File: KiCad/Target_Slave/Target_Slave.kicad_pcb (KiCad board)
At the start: 2 copper layers, 76.2 x 50.8 mm, 44 parts, among them J1 ICSP, J2 I2C, J3 I2C, SW1 I2C Address, U1 PIC16F1788-IP, U2 TSSP4038, U3 TSOP53456

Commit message: Rev B Target Slave PCB design
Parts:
- removed ? (x3): , 
- removed D6: LED, LED_SMD:LED_0805_2012Metric_Pad1.15x1.40mm_HandSolder
- removed the G*** at (135.4, 83.2)
- removed the G*** at (132.0, 118.1)
- removed the G*** at (121.2, 112.8)
- removed R10, R12: 90Ω, Resistor_SMD:R_0805_2012Metric_Pad1.20x1.40mm_HandSolder
- removed R11: 150Ω, Resistor_SMD:R_0805_2012Metric_Pad1.20x1.40mm_HandSolder
- removed R13: 4.7kΩ, Resistor_SMD:R_0805_2012Metric_Pad1.20x1.40mm_HandSolder
- removed R6, R7, R8: 330Ω, Resistor_SMD:R_0805_2012Metric_Pad1.20x1.40mm_HandSolder
- removed R9: 10kΩ, Resistor_SMD:R_0805_2012Metric_Pad1.20x1.40mm_HandSolder
- removed the REF** at (183.6, 81.9)
- removed SW1: I2C Address, 0_AKeller_Footprints:SW_DIP_SPSTx08_Slide_9.78x22.5mm_W7.62mm_P2.54mm
- removed U3: TSOP53456, 0_AKeller_Footprints:IR Receiver
- added C7: 1µF, Capacitor_SMD:C_0805_2012Metric_Pad1.18x1.45mm_HandSolder, F.Cu at (233.9, 81.3)
- added C8: 22uF, Capacitor_SMD:C_0805_2012Metric_Pad1.18x1.45mm_HandSolder, F.Cu at (234.9, 63.9)
- added C9: 0.1uF, Capacitor_SMD:C_0805_2012Metric_Pad1.18x1.45mm_HandSolder, F.Cu at (239.5, 63.9)
- added G***: LOGO, 2025 Logos:AKeller_Logo_0-23x0-31, F.Cu at (243.0, 56.4)
- added G***: LOGO, 2025 Logos:RCET Stacked 0-25x0_76, F.Cu at (218.3, 83.8)
- added J10: I2C, 0_AKeller_Footprints:1x6_100mil_Header, F.Cu at (214.6, 48.9)
- added J4: I2C, 0_AKeller_Footprints:1x6_100mil_Header, F.Cu at (248.9, 70.5)
- added J5: SERVO1, 0_AKeller_Footprints:1x3_100mil_Header, F.Cu at (234.9, 92.1)
- added J6: SERVO3, 0_AKeller_Footprints:1x3_100mil_Header, F.Cu at (234.9, 76.8)
- added J7: SERVO2, 0_AKeller_Footprints:1x3_100mil_Header, F.Cu at (234.9, 84.5)
- added J8: Stepper, 0_AKeller_Footprints:1x4_100mil_Header, F.Cu at (193.0, 92.1)
- added J9: I2C, 0_AKeller_Footprints:1x6_100mil_Header, F.Cu at (214.6, 92.1)
- added JP1: Mode, 0_AKeller_Footprints:1x3_100mil_Jumper, F.Cu at (214.6, 61.6)
- added REF**: M3 Mounting, 0_AKeller_Footprints:M3 Mounting, F.Cu at (180.3, 92.1)
- added REF**: M3 Mounting, 0_AKeller_Footprints:M3 Mounting, F.Cu at (248.9, 92.1)
- added REF**: M3 Mounting, 0_AKeller_Footprints:M3 Mounting, F.Cu at (180.3, 48.9)
- added REF**: M3 Mounting, 0_AKeller_Footprints:M3 Mounting, F.Cu at (248.9, 48.9)
- added TP10: PWR, 0_AKeller_Footprints:1x1_100mil_Header, F.Cu at (239.4, 69.8)
- added TP5: IR, 0_AKeller_Footprints:1x1_100mil_Header, F.Cu at (220.0, 56.9)
- added TP6: TX, 0_AKeller_Footprints:1x1_100mil_Header, F.Cu at (190.0, 59.1)
- added TP7: SCL, 0_AKeller_Footprints:1x1_100mil_Header, F.Cu at (201.8, 85.9)
- added TP8: SDA, 0_AKeller_Footprints:1x1_100mil_Header, F.Cu at (205.6, 85.9)
- added TP9: RX, 0_AKeller_Footprints:1x1_100mil_Header, F.Cu at (207.5, 67.2)
- C4: value 1uF -> 1µF
- C5: value 22uF -> 1µF
- C6: value 0.1uF -> 1µF
- D1: footprint 0_AKeller_Footprints:Diode_0805 -> Diode_SMD:D_0805_2012Metric_Pad1.15x1.40mm_HandSolder
- D2: value IN-P32TRRRGB -> WS2812B; footprint 0_AKeller_Footprints:IN-P32TRRRGB -> LED_SMD:LED_WS2812B_PLCC4_5.0x5.0mm_P3.2mm; moved to F.Cu
- D3: value IN-P32TRRRGB -> Enable; footprint 0_AKeller_Footprints:IN-P32TRRRGB -> LED_SMD:LED_0805_2012Metric_Pad1.15x1.40mm_HandSolder; moved to F.Cu
- D4: value IN-P32TRRRGB -> Hit; footprint 0_AKeller_Footprints:IN-P32TRRRGB -> LED_SMD:LED_0805_2012Metric_Pad1.15x1.40mm_HandSolder; moved to F.Cu
- D5: value IN-P32TRRRGB -> Power; footprint 0_AKeller_Footprints:IN-P32TRRRGB -> LED_SMD:LED_0805_2012Metric_Pad1.15x1.40mm_HandSolder; moved to F.Cu
- J2: value I2C -> LED; footprint 0_AKeller_Footprints:1x4_100mil_Header -> 0_AKeller_Footprints:1x3_100mil_Header_Locking
- J3: footprint 0_AKeller_Footprints:1x4_100mil_Header -> 0_AKeller_Footprints:1x6_100mil_Header
- R1: value 330Ω -> 10kΩ
- R2: value 330Ω -> 470Ω
- R3, R4, R5: value 330Ω -> 4.7kΩ
- TP1: value ~ -> MCLR
- TP2: value ~ -> RGB_IN
- TP3: value ~ -> Enable
- TP4: value ~ -> Hit
- moved C5 115.9 mm to (233.9, 69.8), turned to 0 degrees
- moved R2 114.9 mm to (224.3, 58.5), turned to 0 degrees
- moved D5 107.5 mm to (230.1, 64.9), turned to 0 degrees
- moved D2 105.6 mm to (233.1, 56.9)
- moved TP2 85.9 mm to (202.4, 61.5)
- moved C4 85.2 mm to (233.9, 88.9), turned to 0 degrees
- moved R1 84.4 mm to (188.7, 67.0)
- moved R5 81.6 mm to (224.8, 64.9), turned to 180 degrees
- moved J2 73.6 mm to (235.6, 48.9), turned to 0 degrees
- moved C6 72.5 mm to (197.9, 87.9), turned to 180 degrees
- moved R4 71.6 mm to (187.7, 72.4), turned to 180 degrees
- moved R3 71.1 mm to (187.7, 77.5), turned to 180 degrees
- moved D1 70.7 mm to (196.3, 67.0)
- moved J3 69.5 mm to (180.3, 70.5), turned to -90 degrees
- moved U2 69.3 mm to (220.0, 70.5), turned to -90 degrees
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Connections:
- net RB6 renamed TX
- C4 pad 1: +5V -> GND
- C4 pad 2: GND -> +5V
- C5 pad 1: +5V -> GND
- C5 pad 2: GND -> +5V
- C6 pad 1: +5V -> GND
- C6 pad 2: GND -> +5V
- D1 pad 1: Net-(D1-K) -> /MCLR
- D2 pad 1: Net-(D2-BK) -> +5V
- D2 pad 2: Net-(D2-GK) -> Net-(D2-DOUT)
- D2 pad 3: Net-(D2-RK) -> GND
- D2 pad 4: +5V -> Net-(D2-DIN)
- D3 pad 1: Net-(D2-BK) -> Net-(D3-K)
- D3 pad 2: Net-(D2-GK) -> Net-(D3-A)
- D4 pad 1: Net-(D2-BK) -> Net-(D4-K)
- D4 pad 2: Net-(D2-GK) -> Net-(D4-A)
- D5 pad 1: Net-(D2-BK) -> Net-(D5-K)
- D5 pad 2: Net-(D2-GK) -> +5V
- J1 pad 1: Net-(D1-K) -> /MCLR
- J1 pad 4: RB7 -> RX
- J2 pad 2: Net-(U1-RC3/SCK/SCL) -> Net-(D2-DOUT)
- J2 pad 3: Net-(U1-RC4/SDI/SDA) -> GND
- J3 pad 2: Net-(U1-RC3/SCK/SCL) -> +5V
- J3 pad 3: Net-(U1-RC4/SDI/SDA) -> /SCL
- J3 pad 4: GND -> /SDA
- R1 pad 1: GND -> +5V
- R1 pad 2: /RA0 -> Net-(D1-A)
- R2 pad 1: GND -> Net-(U1-ULPWU/C12IN0-/AN0/RA0)
- R2 pad 2: /RA1 -> Net-(D2-DIN)
- R3 pad 1: GND -> Net-(D3-K)
- R3 pad 2: /RA2 -> GND
- R4 pad 1: GND -> Net-(D4-K)
- R4 pad 2: /RA3 -> GND
- R5 pad 1: GND -> Net-(D5-K)
- R5 pad 2: /RA4 -> GND
- TP1 pad 1: Net-(U1-INT/AN12/RB0) -> /MCLR
- TP2 pad 1: Net-(U1-RC3/SCK/SCL) -> Net-(U1-ULPWU/C12IN0-/AN0/RA0)
- TP3 pad 1: Net-(U1-RC4/SDI/SDA) -> Net-(D3-A)
- TP4 pad 1: Net-(U1-P1C/AN10/RB1) -> Net-(D4-A)
- U1 pad 1: Net-(D1-K) -> /MCLR
- U1 pad 10: /RA6 -> Net-(U1-CLKIN/OSC1/RA7)
- U1 pad 11: unconnected-(U1-RC0/T1OSO/T1CK1-Pad11) -> SERVO1
- U1 pad 13: unconnected-(U1-RC2/P1A/CCP1-Pad13) -> STEP
- U1 pad 14: Net-(U1-RC3/SCK/SCL) -> /SCL
- U1 pad 15: Net-(U1-RC4/SDI/SDA) -> /SDA
- U1 pad 16: unconnected-(U1-RC5/SDO-Pad16) -> SERVO3
- U1 pad 17: unconnected-(U1-RC6/TX/CK-Pad17) -> SERVO2
- U1 pad 2: /RA0 -> Net-(U1-ULPWU/C12IN0-/AN0/RA0)
- U1 pad 21: Net-(U1-INT/AN12/RB0) -> unconnected-(U1-INT/AN12/RB0-Pad21)
- U1 pad 22: Net-(U1-P1C/AN10/RB1) -> unconnected-(U1-P1C/AN10/RB1-Pad22)
- U1 pad 23: Net-(U1-P1B/AN8/RB2) -> unconnected-(U1-P1B/AN8/RB2-Pad23)
- U1 pad 24: Net-(U1-PGM/C12IN2-/AN8/RB3) -> unconnected-(U1-PGM/C12IN2-/AN8/RB3-Pad24)
- U1 pad 25: Net-(U1-P1D/AN11/RB4) -> unconnected-(U1-P1D/AN11/RB4-Pad25)
- U1 pad 28: RB7 -> Net-(JP1-C)
- U1 pad 3: /RA1 -> Net-(D4-A)
- U1 pad 4: /RA2 -> Net-(D3-A)
- U1 pad 5: /RA3 -> DIR
- U1 pad 6: /RA4 -> unconnected-(U1-T0CKI/C1OUT/RA4-Pad6)
- U1 pad 7: /RA5 -> unconnected-(U1-~{SS}/C2OUT/AN4/RA5-Pad7)
- U1 pad 9: /RA7 -> Net-(U1-CLKIN/OSC1/RA7)
- U2 pad 1: Net-(U1-INT/AN12/RB0) -> Net-(JP1-A)
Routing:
- net /SDA: track 0.00 -> 201.2 mm
- net /SCL: track 0.00 -> 193.1 mm
- net Net-(U1-RC3/SCK/SCL): track 151.6 -> 0.00 mm
- net Net-(U1-RC4/SDI/SDA): track 133.8 -> 0.00 mm
- net Net-(D2-GK): track 97.1 -> 0.00 mm, vias 1 -> 0
- net Net-(D2-RK): track 95.8 -> 0.00 mm
- net Net-(D2-BK): track 92.1 -> 0.00 mm, vias 1 -> 0
- net +5V: track 280.4 -> 226.8 mm
- net SERVO1: track 0.00 -> 43.0 mm
- net Net-(D1-K): track 41.8 -> 0.00 mm
- net SERVO2: track 0.00 -> 40.0 mm
- net Net-(U1-ULPWU/C12IN0-/AN0/RA0): track 0.00 -> 37.3 mm
- net /MCLR: track 0.00 -> 36.0 mm
- net RB7: track 35.2 -> 0.00 mm
- net /RA7: track 31.8 -> 0.00 mm, vias 1 -> 0
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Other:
- board text added: "Game"
- board text added: "Laser Arcade Target Slave Rev. B - Fall 2025"
- board text added: "PGM"
- board text added: "SIG"
- board text removed: "D2"
- board text removed: "D3"
- board text removed: "D4"
- board text removed: "D5"
- board text removed: "I2C"
- board text removed: "ICSP"
- board text removed: "Laser Arcade Target Slave Rev. A Spring 2025"

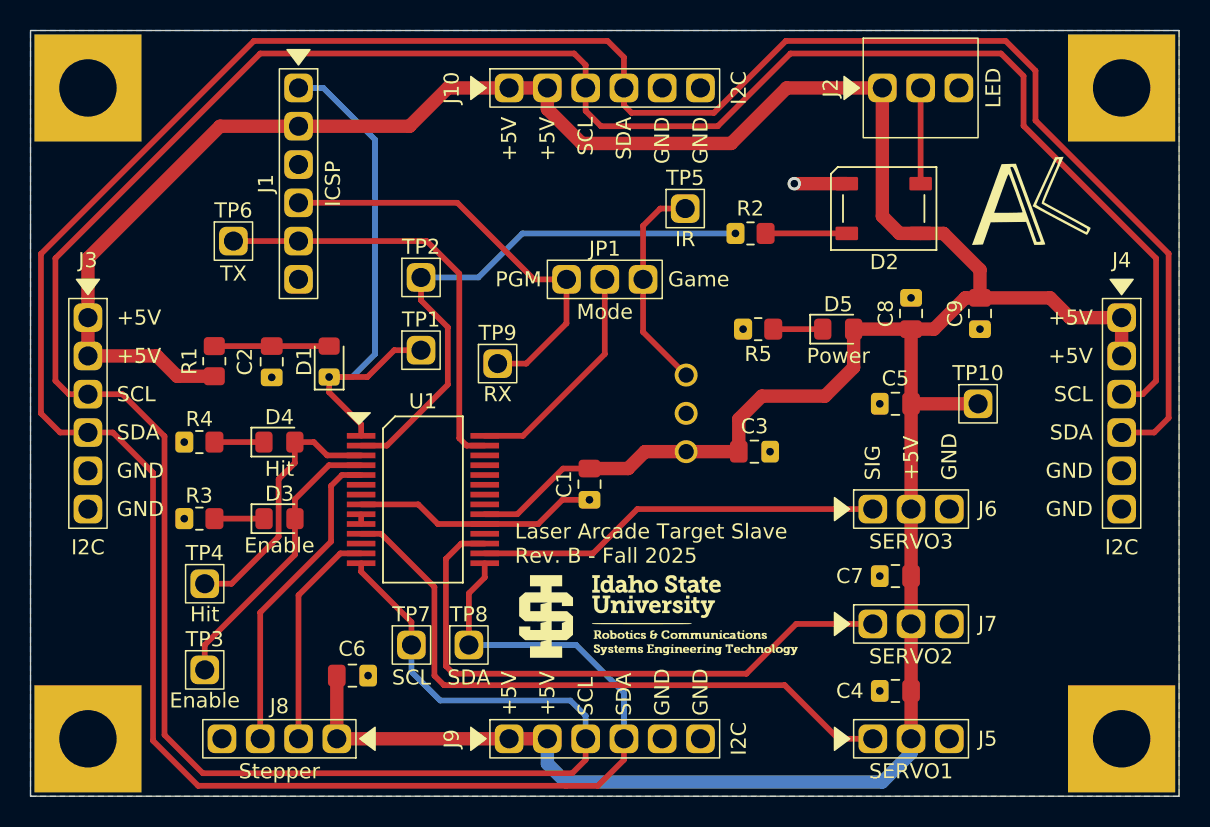
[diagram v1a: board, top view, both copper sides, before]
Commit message: Plot Target Slave Gerbers
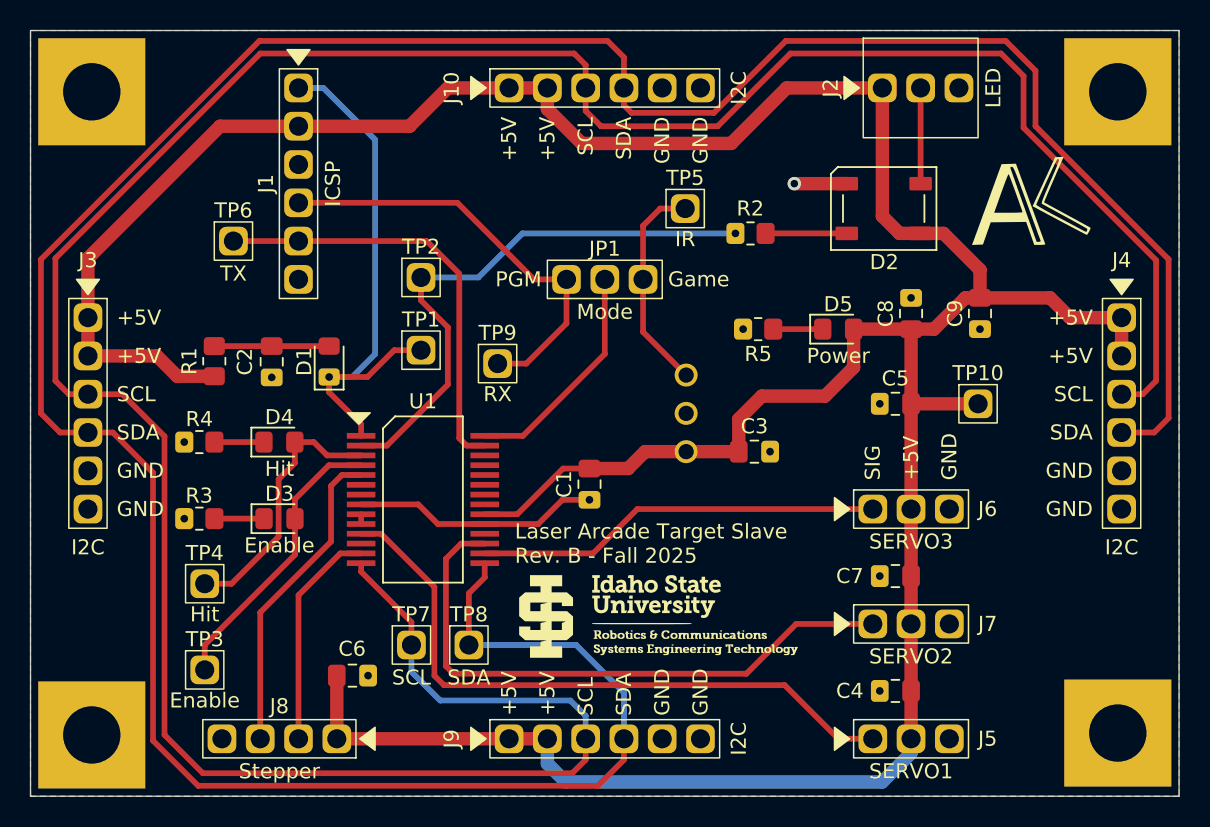
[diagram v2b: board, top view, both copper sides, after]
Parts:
- moved REF** 0.46 mm to (248.7, 91.7)
- moved REF** 0.36 mm to (180.6, 91.8)
- moved REF** 0.36 mm to (180.6, 49.1)
- moved REF** 0.36 mm to (248.7, 49.1)
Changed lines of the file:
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@@
 			(drillshape 0)
 			(scaleselection 1)
-			(outputdirectory "Slave_Gerbers/")
+			(outputdirectory "Target_Slave_RevB/Gerbers/")
 		)
 	)
@@
 	)
 	(footprint "0_AKeller_Footprints:M3 Mounting"
+		(locked yes)
 		(layer "F.Cu")
-		(at 180.34 92.075)
+		(at 180.594 91.821)
 		(property "Reference" "REF**"
 			(at 0 -0.5 0)
@@
 	)
 	(footprint "0_AKeller_Footprints:M3 Mounting"
+		(locked yes)
 		(layer "F.Cu")
-		(at 248.92 92.075)
+		(at 248.666 91.694)
 		(property "Reference" "REF**"
 			(at 0 -0.5 0)
@@
 	(footprint "0_AKeller_Footprints:M3 Mounting"
 		(layer "F.Cu")
-		(at 180.34 48.895)
+		(at 180.594 49.149)
 		(property "Reference" "REF**"
 			(at 0 -0.5 0)
@@
 	(footprint "0_AKeller_Footprints:M3 Mounting"
 		(layer "F.Cu")
-		(at 248.92 48.895)
+		(at 248.666 49.149)
 		(property "Reference" "REF**"
 			(at 0 -0.5 0)
@@
 	)
 	(segment
-		(start 180.34 69.215)
-		(end 179.07 69.215)
+		(start 240.919 46.609)
+		(end 242.412464 48.102464)
 		(width 0.381)
 		(layer "F.Cu")
@@
 	)
 	(segment
-		(start 251.206 68.326)
-		(end 250.317 69.215)
+		(start 180.34 69.215)
+		(end 179.07 69.215)
 		(width 0.381)
 		(layer "F.Cu")
@@
 	)
 	(segment
-		(start 222.123 51.435)
-		(end 226.949 46.609)
+		(start 226.949 46.609)
+		(end 240.919 46.609)
 		(width 0.381)
 		(layer "F.Cu")
@@
 	)
 	(segment
-		(start 226.949 46.609)
-		(end 240.919 46.609)
-		(width 0.381)
-		(layer "F.Cu")
-		(net 33)
-	)
-	(segment
-		(start 213.36 48.895)
-		(end 213.36 50.419)
+		(start 185.42 72.009)
+		(end 185.42 91.821)
 		(width 0.381)
 		(layer "F.Cu")
@@
 	)
 	(segment
-		(start 185.42 72.009)
-		(end 185.42 91.821)
+		(start 242.412464 51.531464)
+		(end 251.206 60.325)
 		(width 0.381)
 		(layer "F.Cu")
@@
 	)
 	(segment
-		(start 251.206 60.198)
-		(end 251.206 68.326)
+		(start 251.206 68.326)
+		(end 250.317 69.215)
 		(width 0.381)
 		(layer "F.Cu")
@@
 	)
 	(segment
-		(start 242.412464 48.102464)
-		(end 242.412464 51.404464)
+		(start 213.36 48.895)
+		(end 213.36 50.419)
 		(width 0.381)
 		(layer "F.Cu")
@@
 	)
 	(segment
-		(start 242.412464 51.404464)
-		(end 251.206 60.198)
+		(start 185.42 91.821)
+		(end 187.96 94.361)
 		(width 0.381)
 		(layer "F.Cu")
@@
 	)
 	(segment
-		(start 185.42 91.821)
-		(end 187.96 94.361)
+		(start 212.471 94.361)
+		(end 213.36 93.472)
 		(width 0.381)
 		(layer "F.Cu")
@@
 	)
 	(segment
-		(start 214.376 51.435)
-		(end 222.123 51.435)
+		(start 182.626 69.215)
+		(end 185.42 72.009)
 		(width 0.381)
 		(layer "F.Cu")
@@
 	)
 	(segment
-		(start 212.471 94.361)
-		(end 213.36 93.472)
+		(start 242.412464 48.102464)
+		(end 242.412464 51.531464)
 		(width 0.381)
 		(layer "F.Cu")
@@
 	)
 	(segment
-		(start 182.626 69.215)
-		(end 185.42 72.009)
+		(start 213.36 47.371)
+		(end 213.36 48.895)
 		(width 0.381)
 		(layer "F.Cu")
@@
 	)
 	(segment
-		(start 213.36 50.419)
-		(end 214.376 51.435)
+		(start 191.77 46.609)
+		(end 212.598 46.609)
 		(width 0.381)
 		(layer "F.Cu")
@@
 	)
 	(segment
-		(start 213.36 47.371)
-		(end 213.36 48.895)
+		(start 214.376 51.435)
+		(end 222.123 51.435)
 		(width 0.381)
 		(layer "F.Cu")
@@
 	)
 	(segment
-		(start 240.919 46.609)
-		(end 242.412464 48.102464)
+		(start 213.36 50.419)
+		(end 214.376 51.435)
 		(width 0.381)
 		(layer "F.Cu")
@@
 	)
 	(segment
-		(start 191.77 46.609)
-		(end 212.598 46.609)
+		(start 250.317 69.215)
+		(end 248.92 69.215)
 		(width 0.381)
 		(layer "F.Cu")
@@
 	)
 	(segment
-		(start 250.317 69.215)
-		(end 248.92 69.215)
+		(start 201.803 84.328)
+		(end 198.465001 80.990001)
 		(width 0.381)
 		(layer "F.Cu")
@@
 	)
 	(segment
-		(start 201.803 84.328)
-		(end 198.465001 80.990001)
+		(start 251.206 60.325)
+		(end 251.206 68.326)
+		(width 0.381)
+		(layer "F.Cu")
+		(net 33)
+	)
+	(segment
+		(start 222.123 51.435)
+		(end 226.949 46.609)
 		(width 0.381)
 		(layer "F.Cu")
@@
 	)
 	(segment
-		(start 191.3535 45.7765)
-		(end 214.8135 45.7765)
+		(start 177.2215 60.2685)
+		(end 191.7135 45.7765)
 		(width 0.381)
 		(layer "F.Cu")
@@
 	)
 	(segment
-		(start 215.9 46.863)
-		(end 215.9 48.895)
+		(start 181.991 71.755)
+		(end 184.658 74.422)
 		(width 0.381)
 		(layer "F.Cu")
@@
 	)
 	(segment
-		(start 243.205 47.752)
-		(end 243.205 51.054)
+		(start 206.664999 80.425)
+		(end 206.664999 81.371001)
 		(width 0.381)
 		(layer "F.Cu")
@@
 	)
 	(segment
-		(start 206.664999 80.425)
-		(end 206.664999 81.371001)
+		(start 243.205 47.752)
+		(end 243.205 51.435)
 		(width 0.381)
 		(layer "F.Cu")
@@
 	)
 	(segment
-		(start 180.34 71.755)
-		(end 178.4915 71.755)
+		(start 184.658 92.202)
+		(end 187.6495 95.1935)
 		(width 0.381)
 		(layer "F.Cu")
@@
 	)
 	(segment
-		(start 180.34 71.755)
-		(end 181.991 71.755)
+		(start 205.613 82.423)
+		(end 205.613 85.852)
 		(width 0.381)
 		(layer "F.Cu")
@@
 	)
 	(segment
-		(start 241.2295 45.7765)
-		(end 243.205 47.752)
+		(start 252.0385 60.2685)
+		(end 252.0385 70.7955)
 		(width 0.381)
 		(layer "F.Cu")
@@
 	)
 	(segment
-		(start 205.613 82.423)
-		(end 205.613 85.852)
+		(start 215.9 48.895)
+		(end 215.9 50.038)
 		(width 0.381)
 		(layer "F.Cu")
@@
 	)
 	(segment
-		(start 184.658 92.202)
-		(end 187.6495 95.1935)
+		(start 191.7135 45.7765)
+		(end 214.8135 45.7765)
 		(width 0.381)
 		(layer "F.Cu")
@@
 	)
 	(segment
-		(start 178.4915 71.755)
-		(end 177.2215 70.485)
+		(start 180.34 71.755)
+		(end 181.991 71.755)
 		(width 0.381)
 		(layer "F.Cu")
@@
 	)
 	(segment
-		(start 177.2215 70.485)
-		(end 177.2215 59.9085)
+		(start 216.408 50.546)
+		(end 221.869 50.546)
 		(width 0.381)
 		(layer "F.Cu")
@@
 	)
 	(segment
-		(start 184.658 74.422)
-		(end 184.658 92.202)
+		(start 214.1785 95.1935)
+		(end 215.9 93.472)
 		(width 0.381)
 		(layer "F.Cu")
@@
 	)
 	(segment
-		(start 215.9 50.038)
-		(end 216.408 50.546)
+		(start 214.8135 45.7765)
+		(end 215.9 46.863)
 		(width 0.381)
 		(layer "F.Cu")
@@
 	)
 	(segment
-		(start 215.9 48.895)
-		(end 215.9 50.038)
+		(start 241.2295 45.7765)
+		(end 243.205 47.752)
 		(width 0.381)
 		(layer "F.Cu")
@@
 	)
 	(segment
-		(start 181.991 71.755)
-		(end 184.658 74.422)
+		(start 184.658 74.422)
+		(end 184.658 92.202)
 		(width 0.381)
 		(layer "F.Cu")
@@
 	)
 	(segment
-		(start 221.869 50.546)
-		(end 226.6385 45.7765)
+		(start 178.4915 71.755)
+		(end 177.2215 70.485)
 		(width 0.381)
 		(layer "F.Cu")
@@
 	)
 	(segment
-		(start 243.205 51.054)
-		(end 252.0385 59.8875)
+		(start 215.9 93.472)
+		(end 215.9 92.075)
 		(width 0.381)
 		(layer "F.Cu")
@@
 	)
 	(segment
-		(start 177.2215 59.9085)
-		(end 191.3535 45.7765)
+		(start 215.9 46.863)
+		(end 215.9 48.895)
 		(width 0.381)
 		(layer "F.Cu")
@@
 	)
 	(segment
-		(start 216.408 50.546)
-		(end 221.869 50.546)
+		(start 252.0385 70.7955)
+		(end 251.079 71.755)
 		(width 0.381)
 		(layer "F.Cu")
@@
 	)
 	(segment
-		(start 252.0385 59.8875)
-		(end 252.0385 70.7955)
+		(start 180.34 71.755)
+		(end 178.4915 71.755)
 		(width 0.381)
 		(layer "F.Cu")
@@
 	)
 	(segment
-		(start 214.8135 45.7765)
-		(end 215.9 46.863)
+		(start 177.2215 70.485)
+		(end 177.2215 60.2685)
 		(width 0.381)
 		(layer "F.Cu")
@@
 	)
 	(segment
-		(start 215.9 93.472)
-		(end 215.9 92.075)
+		(start 221.869 50.546)
+		(end 226.6385 45.7765)
 		(width 0.381)
 		(layer "F.Cu")
@@
 	)
 	(segment
-		(start 252.0385 70.7955)
-		(end 251.079 71.755)
+		(start 243.205 51.435)
+		(end 252.0385 60.2685)
 		(width 0.381)
 		(layer "F.Cu")
@@
 	)
 	(segment
-		(start 214.1785 95.1935)
-		(end 215.9 93.472)
+		(start 215.9 50.038)
+		(end 216.408 50.546)
 		(width 0.381)
 		(layer "F.Cu")

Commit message: Completed Target Master PCB, export gerbers and views
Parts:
- moved C2 76.9 mm to (119.0, 89.3)
- moved D1 76.9 mm to (122.8, 89.3)
- moved D3 76.9 mm to (119.5, 99.7)
- moved R1 76.9 mm to (115.2, 89.3)
- moved C1 76.9 mm to (140.0, 97.4)
- moved C3 76.9 mm to (151.0, 95.3)
- moved C4 76.9 mm to (160.3, 111.2)
- moved C5 76.9 mm to (160.3, 92.1)
- moved C7 76.9 mm to (160.3, 103.5)
- moved C8 76.9 mm to (161.4, 86.1)
- moved C9 76.9 mm to (166.0, 86.1)
- moved D2 76.9 mm to (159.6, 79.2)
- moved D4 76.9 mm to (119.5, 94.6)
- moved D5 76.9 mm to (156.6, 87.2)
- moved G*** 76.9 mm to (169.4, 78.6)
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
